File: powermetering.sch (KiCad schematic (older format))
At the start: 181 parts, among them J1 Conn_01x04, J12 CONN_01X02, J13 CONN_01X02, J14 CONN_01X02, J15 CONN_01X02, J2 Conn_01x02, J3 Conn_01x02, J4 Conn_01x02, J5 Conn_01x02, J7 CONN_01X02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

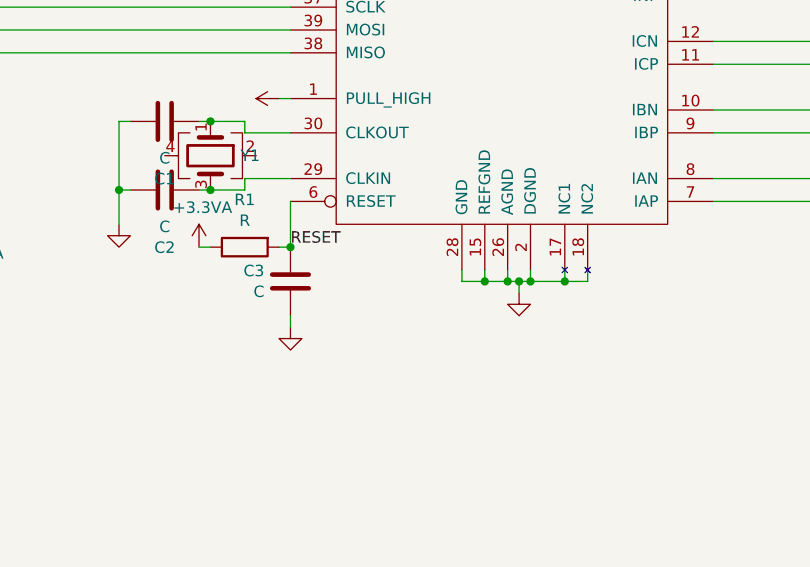
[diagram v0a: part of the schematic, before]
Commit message: add ade reset jumper
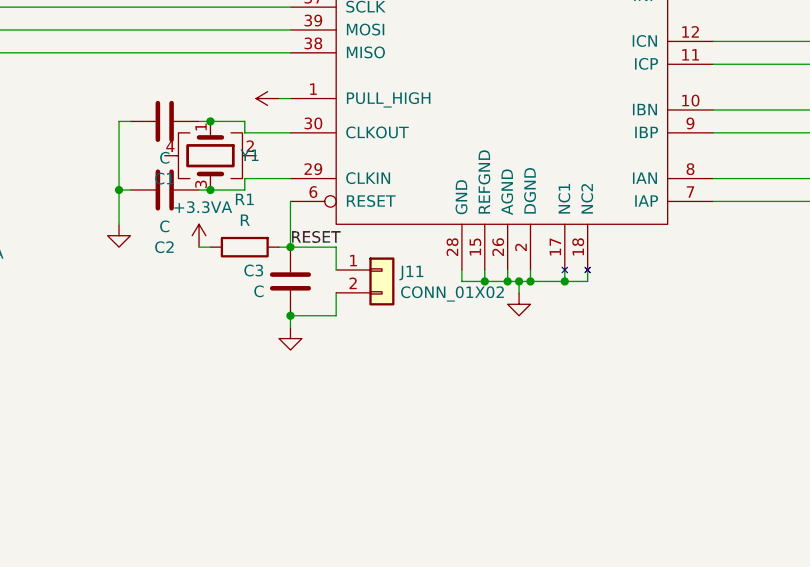
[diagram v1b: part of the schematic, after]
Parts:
- added J11: CONN_01X02, stmbl:Pin_Header_Straight_1x02, symbol stmbl:CONN_01X02
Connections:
- net GNDA: now also J11.2 (Pin_2)
- net RESET: now also J11.1 (Pin_1)
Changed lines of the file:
@@
 Wire Wire Line
 	2250 4400 2300 4400
+$Comp
+L stmbl:CONN_01X02 J11
+U 1 1 5D1FE2E5
+P 9050 6900
+F 0 "J11" H 9130 6892 50  0000 L CNN
+F 1 "CONN_01X02" H 9130 6801 50  0000 L CNN
+F 2 "stmbl:Pin_Header_Straight_1x02" H 9050 6900 50  0001 C CNN
+F 3 "" H 9050 6900 50  0001 C CNN
+	1    9050 6900
+	1    0    0    -1
+$EndComp
+Wire Wire Line
+	8650 6800 8850 6800
+Wire Wire Line
+	8850 6800 8850 6900
+Wire Wire Line
+	8650 7100 8850 7100
+Wire Wire Line
+	8850 7100 8850 7000
+Connection ~ 8650 7100
 $EndSCHEMATC

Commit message: small changes
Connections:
- net GNDS: now also D21.3 (~~)
- net L2: no longer D21.4 (~~)
- net L3: now also D21.4 (~~); no longer D21.3 (~~)
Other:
- moved on the sheet: D21
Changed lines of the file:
@@
 L Diode_Bridge:ABS10 D21
 U 1 1 5D6C9DAC
-P 1950 2400
-F 0 "D21" H 2294 2446 50  0000 L CNN
-F 1 "ABS10" H 2294 2355 50  0000 L CNN
-F 2 "Diode_SMD:Diode_Bridge_Diotec_ABS" H 2100 2525 50  0001 L CNN
-F 3 "https://diotec.com/tl_files/diotec/files/pdf/datasheets/abs2.pdf" H 1950 2400 50  0001 C CNN
-	1    1950 2400
+P 1950 3000
+F 0 "D21" H 2294 3046 50  0000 L CNN
+F 1 "ABS10" H 2294 2955 50  0000 L CNN
+F 2 "Diode_SMD:Diode_Bridge_Diotec_ABS" H 2100 3125 50  0001 L CNN
+F 3 "https://diotec.com/tl_files/diotec/files/pdf/datasheets/abs2.pdf" H 1950 3000 50  0001 C CNN
+	1    1950 3000
 	1    0    0    -1
 $EndComp
@@
 Wire Wire Line
 	1950 2050 1950 2000
-Wire Wire Line
-	1950 2050 1950 2100
-Connection ~ 1950 2050
 Wire Wire Line
 	1050 2700 1300 2700
@@
 Connection ~ 2250 1900
 Wire Wire Line
-	2250 1900 2250 2400
-Wire Wire Line
 	1650 2150 2900 2150
 Wire Wire Line
 	2900 2150 2900 2400
 Connection ~ 1650 2150
-Wire Wire Line
-	1650 2150 1650 2400
 $Sheet
 S 8550 900  1250 1450
@@
 	8850 7100 8850 7000
 Connection ~ 8650 7100
+Wire Wire Line
+	1050 3300 1950 3300
+Wire Wire Line
+	1650 2150 1650 3000
+Wire Wire Line
+	2250 1900 2250 3000
+$Comp
+L power:GNDS #PWR?
+U 1 1 5D22A16B
+P 1050 3300
+F 0 "#PWR?" H 1050 3050 50  0001 C CNN
+F 1 "GNDS" H 1055 3127 50  0000 C CNN
+F 2 "" H 1050 3300 50  0001 C CNN
+F 3 "" H 1050 3300 50  0001 C CNN
+	1    1050 3300
+	1    0    0    -1
+$EndComp
 $EndSCHEMATC

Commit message: small production changes
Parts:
- removed C27, C28, C29, C30, C31, C32, C33, C34: C, stmbl:C_0603, symbol stmbl:C
- removed R14, R15, R16, R17, R18, R19, R20, R21: 1k, stmbl:R_0603, symbol stmbl:R
- added C27: 470µ, Capacitor_SMD:CP_Elec_6.3x5.9, symbol stmbl:CP
- H1, H10, H11, H12, H13, H14, H15, H16, H2, H3, H4, H9: footprint MountingHole:MountingHole_3.2mm_M3 -> MountingHole:MountingHole_5.5mm
- J1: footprint TerminalBlock_Phoenix:TerminalBlock_Phoenix_PT-1,5-5-5.0-H_1x05_P5.00mm_Horizontal -> stmbl:RM5.08_1x5_UP
- J2, J3, J4, J5: footprint TerminalBlock_Phoenix:TerminalBlock_Phoenix_PT-1,5-2-5.0-H_1x02_P5.00mm_Horizontal -> stmbl:RM5.08_1x2_UP
- R10, R11, R12, R13, R6, R7, R8, R9: value 0R -> 1k
- R25, R26, R27, R28, R29, R30, R31, R32, R33, R42, R43, R44: footprint Resistor_SMD:R_2010_5025Metric -> stmbl:R_1206
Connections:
- net +3.3VA: now also C27.1
- net GNDA: now also C27.2
- net at D2.1 (A), D2.2 (K), J2.1 (Pin_1)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: now also R6.2
- net at D3.1 (A), D3.2 (K), J2.2 (Pin_2)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: now also R7.2
- net at D4.1 (A), D4.2 (K), J3.1 (Pin_1)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: now also R8.2
- net at D5.1 (A), D5.2 (K), J3.2 (Pin_2)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: now also R9.2
- net at D6.1 (A), D6.2 (K), J4.1 (Pin_1)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: now also R10.2
- net at D7.1 (A), D7.2 (K), J4.2 (Pin_2)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: now also R11.2
- net at D8.1 (A), D8.2 (K), J5.1 (Pin_1)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: now also R12.2
- net at D9.1 (A), D9.2 (K), J5.2 (Pin_2)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: now also R13.2
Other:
- moved on the sheet: D2, D3, D4, D5, D6, D7, D8, D9, J2, J3, J4, J5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

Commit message: fix SD card socket, move around psu stuff
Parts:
- TR2: symbol altair04:TRANSFO -> powermetering-rescue:TRANSFO-altair04
- U5: symbol altair04:ALTAIR04-900 -> powermetering-rescue:ALTAIR04-900-altair04
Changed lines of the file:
@@
 EESchema Schematic File Version 5
 LIBS:powermetering-cache
-EELAYER 29 0
+EELAYER 30 0
 EELAYER END
 $Descr A3 16535 11693
@@
 Comment3 ""
 Comment4 ""
+Comment5 ""
+Comment6 ""
+Comment7 ""
+Comment8 ""
+Comment9 ""
 $EndDescr
 $Comp
@@
 $EndComp
 $Comp
-L altair04:TRANSFO TR2
+L powermetering-rescue:TRANSFO-altair04 TR2
 U 1 1 5CF1BE92
 P 3850 4050
@@
 	3300 4600 3300 4700
 $Comp
-L altair04:ALTAIR04-900 U5
+L powermetering-rescue:ALTAIR04-900-altair04 U5
 U 1 1 5CF1BEA7
 P 2550 5000

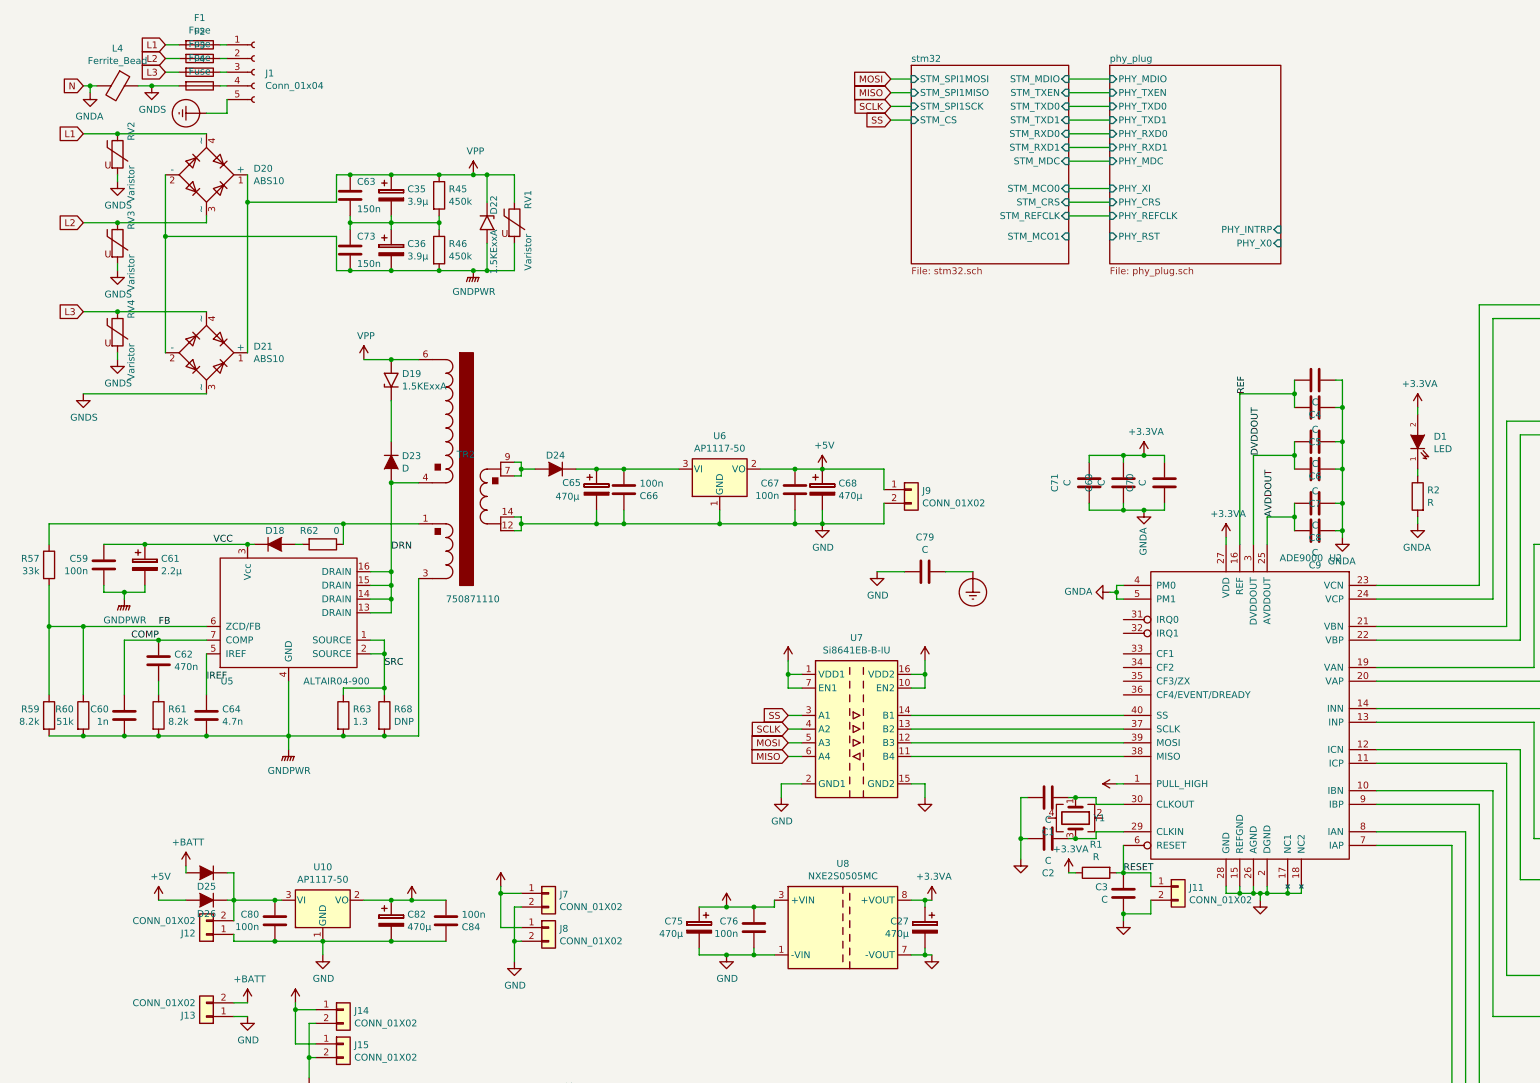
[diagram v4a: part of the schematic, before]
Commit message: remove eight pulse rectifier, add three pulse rectifier with artificial star point
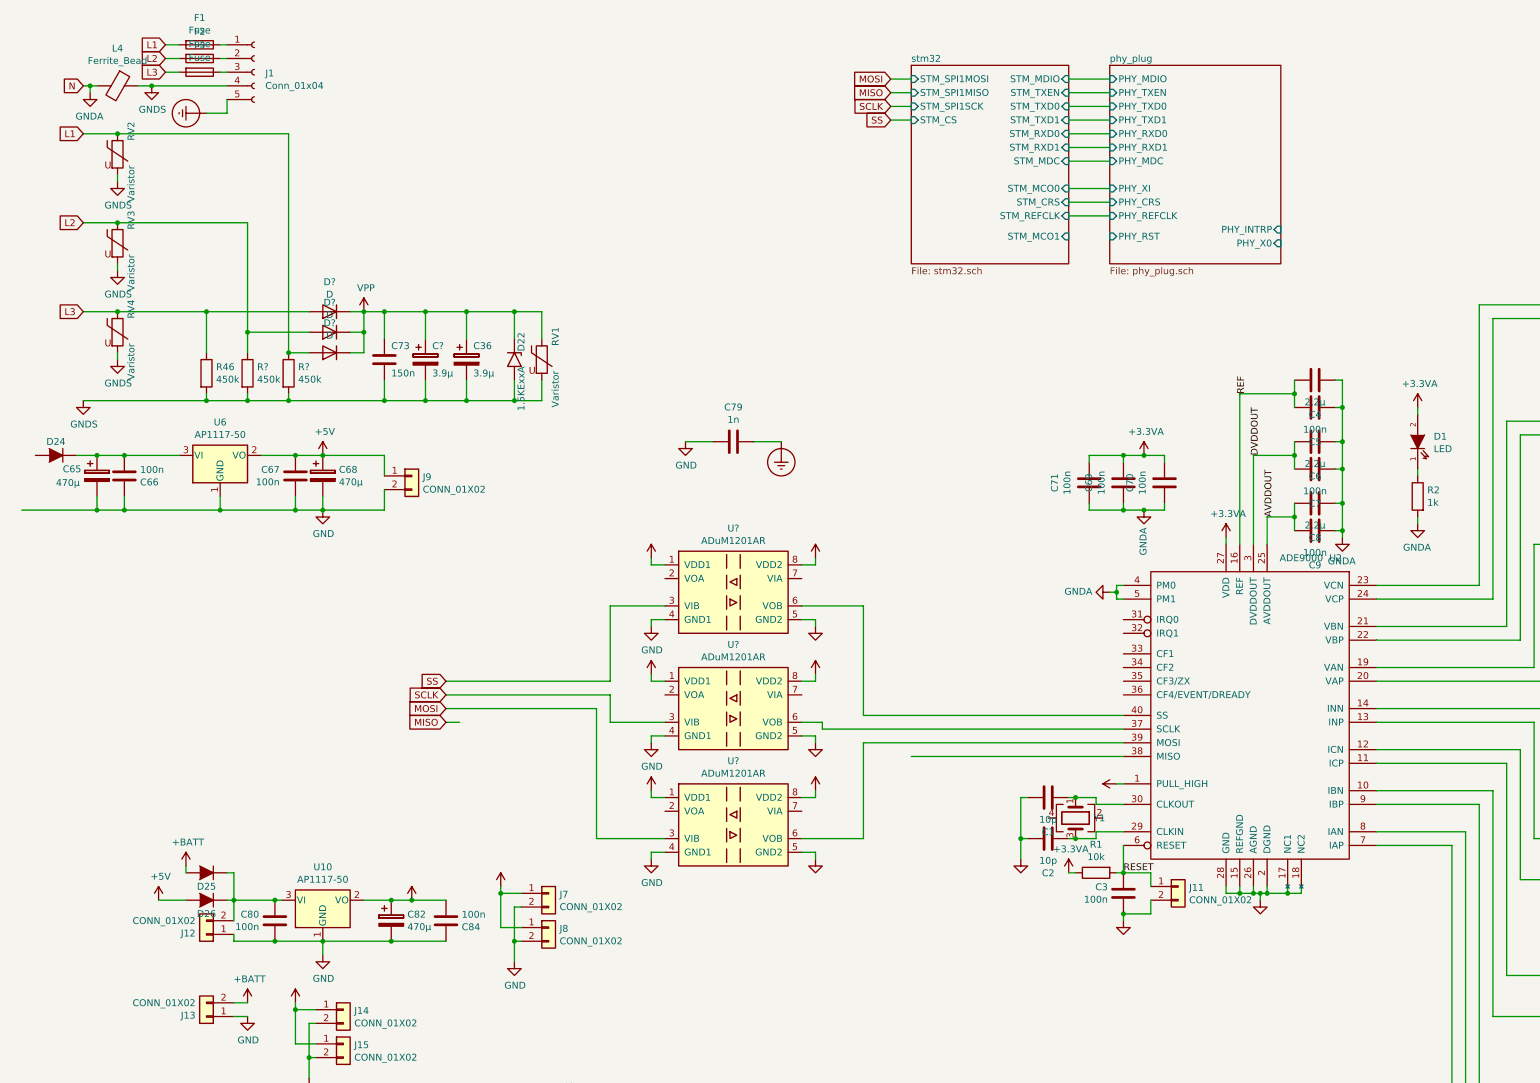
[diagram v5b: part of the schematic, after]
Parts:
- removed C27: 470µ, Capacitor_SMD:CP_Elec_6.3x5.9, symbol stmbl:CP
- removed C35: 3.9µ, Capacitor_SMD:CP_Elec_8x10, symbol stmbl:CP
- removed C59, C76: 100n, stmbl:C_0805, symbol stmbl:C
- removed C60: 1n, stmbl:C_0805, symbol stmbl:C
- removed C61: 2.2µ, stmbl:C_1206, symbol stmbl:CP
- removed C62: 470n, stmbl:C_0805, symbol stmbl:C
- removed C63: 150n, stmbl:C_1808, symbol stmbl:C
- removed C64: 4.7n, stmbl:C_0805, symbol stmbl:C
- removed C75: 470µ, Capacitor_SMD:CP_Elec_8x10.5, symbol stmbl:CP
- removed D18, D23: D, stmbl:SMA_Standard, symbol stmbl:D
- removed D19: 1.5KExxA, Diode_SMD:D_SMC, symbol Diode:1.5KExxA
- removed D20, D21: ABS10, Diode_SMD:Diode_Bridge_Diotec_ABS, symbol Diode_Bridge:ABS10
- removed F4: Fuse, Fuse:Fuse_SunFuse-6HP, symbol Device:Fuse
- removed R45: 450k, stmbl:R_1206, symbol stmbl:R
- removed R57: 33k, stmbl:R_0805, symbol stmbl:R
- removed R59, R61: 8.2k, stmbl:R_0805, symbol stmbl:R
- removed R60: 51k, stmbl:R_0805, symbol stmbl:R
- removed R62: 0, stmbl:R_0805, symbol stmbl:R
- removed R63: 1.3, stmbl:R_1206, symbol stmbl:R
- removed R68: DNP, stmbl:R_1206, symbol stmbl:R
- removed TR2: 750871110, altair04:750871110, symbol powermetering-rescue:TRANSFO-altair04
- removed U5: ALTAIR04-900, Package_SO:SOIC-16_3.9x9.9mm_P1.27mm, symbol powermetering-rescue:ALTAIR04-900-altair04
- removed U7: Si8641EB-B-IU, Package_SO:QSOP-16_3.9x4.9mm_P0.635mm, symbol Isolator:Si8641EB-B-IU
- removed U8: NXE2S0505MC, Converter_DCDC:Converter_DCDC_muRata_NXE2SxxxxMC_THT, symbol Regulator_Switching:NXE2S0505MC
- added C?: 3.9µ, Capacitor_SMD:CP_Elec_8x10, symbol stmbl:CP
- added D? (x3): D, symbol Device:D
- added R? (x2): 450k, stmbl:R_1206, symbol stmbl:R
- added U? (x3): ADuM1201AR, Package_SO:SOIC-8_3.9x4.9mm_P1.27mm, symbol Isolator:ADuM1201AR
- C1, C2: value C -> 10p
- C3, C5, C69, C7, C70, C71, C9: value C -> 100n
- C4, C6, C8: value C -> 2.2µ
- C79: value C -> 1n
- R1: value R -> 10k
- R2: value R -> 1k
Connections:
- net GNDPWR is gone; now on net GNDS: C36.2, C73.2, D22.2 (A2), R46.2, RV1.2
- net +3.3VA: now also U?.8 (VDD2), U?.8 (VDD2), U?.8 (VDD2)
- net +3V3: now also U?.1 (VDD1), U?.1 (VDD1), U?.1 (VDD1)
- net GND: now also U?.4 (GND1), U?.4 (GND1), U?.4 (GND1)
- net GNDA: now also U?.5 (GND2), U?.5 (GND2), U?.5 (GND2)
- net GNDS: now also J1.4 (Pin_4), C?.2, R?.2, R?.2
- net L1: now also D?.2 (A), R?.1
- net L2: now also D?.2 (A), R?.1
- net L3: now also R46.1, D?.2 (A)
- net MOSI: now also U?.3 (VIB)
- net SCLK: now also U?.3 (VIB)
- net SS: now also U?.3 (VIB)
- net VPP: now also C36.1, C73.1, C?.1, D?.1 (K), D?.1 (K), D?.1 (K)
- net at U2.37 (SCLK): now also U?.6 (VOB)
- net at U2.39 (MOSI): now also U?.6 (VOB)
- net at U2.40 (SS): now also U?.6 (VOB)
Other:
- moved on the sheet: C36, C65, C66, C67, C68, C73, C79, D22, D24, J9, R46, RV1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
